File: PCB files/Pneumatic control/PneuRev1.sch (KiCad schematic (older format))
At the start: 52 parts, among them J1 SIG_IN, J2 BATT_IN, J3 PNEU, U1 uA7824, U2 OP279, U3 OP279, U4 OP279, U5 OP279, U6 OP279, U7 OP279, U8 OP07

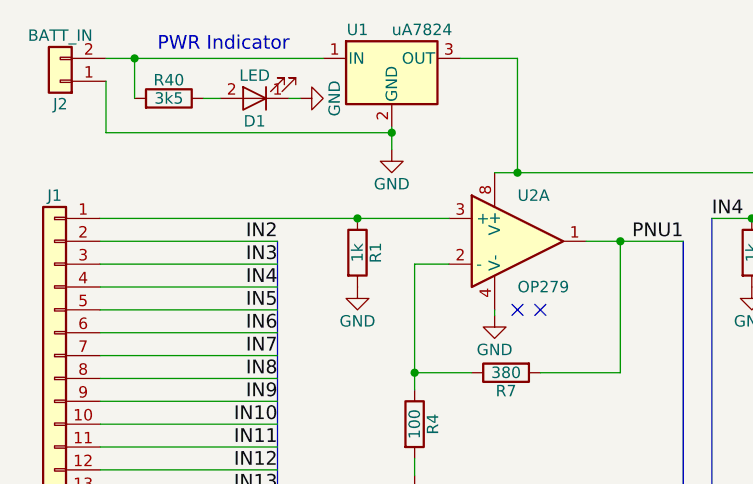
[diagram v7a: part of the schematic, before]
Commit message: 2/4/2019
-Fixed schematic opamp numbering issue
-Relabelled LED limit resistor to 3k
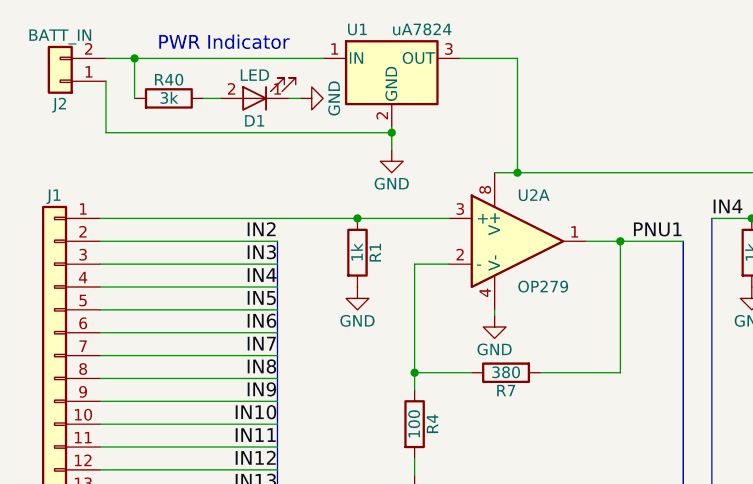
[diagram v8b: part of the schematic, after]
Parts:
- R40: value 3k5 -> 3k
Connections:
- no-connect marks 26 -> 24
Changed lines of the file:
@@
 	-1   0    0    1
 $EndComp
-NoConn ~ 2900 1800
-NoConn ~ 3000 1800
 Wire Wire Line
 	3200 1500 3625 1500
@@
 P 1375 875
 F 0 "R40" V 1455 875 50  0000 C CNN
-F 1 "3k5" V 1375 875 50  0000 C CNN
+F 1 "3k" V 1375 875 50  0000 C CNN
 F 2 "Resistors_THT:R_Axial_DIN0204_L3.6mm_D1.6mm_P5.08mm_Horizontal" V 1305 875 50  0001 C CNN
 F 3 "" H 1375 875 50  0001 C CNN
